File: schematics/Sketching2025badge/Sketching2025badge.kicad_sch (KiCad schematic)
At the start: 47 parts, among them J1 Conn_02x03, J2 Conn_01x04_Pin, SW1 Capacitive_Button, SW10 SSSS811101, SW2 Capacitive_Button, SW3 Capacitive_Button, U1 ATtiny816-M

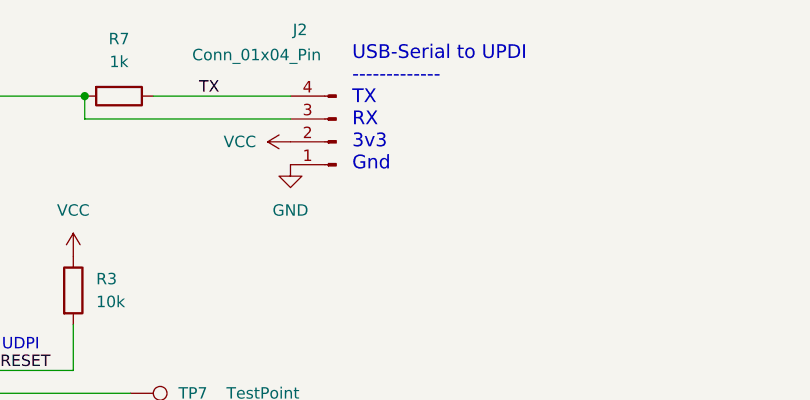
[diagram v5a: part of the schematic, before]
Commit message: moved to female prog header, widened mask polygons for more light
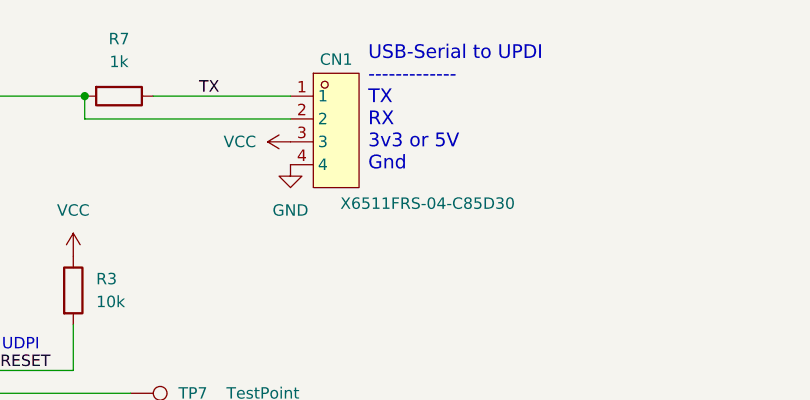
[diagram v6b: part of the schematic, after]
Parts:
- removed J2: Conn_01x04_Pin, Connector_Harwin:Harwin_M20-89004xx_1x04_P2.54mm_Horizontal, symbol Connector:Conn_01x04_Pin
- added CN1: X6511FRS-04-C85D30, easyeda2kicad:HDR-SMD_4P-P2.54-H-F, symbol easyeda2kicad:X6511FRS-04-C85D30
- J1: LCSC Part (none) -> C541853
- SW1, SW2, SW3, TP1, TP2, TP3, TP4: now left out of the parts list
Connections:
- net GND: now also CN1.4
- net RESET: now also CN1.2
- net TX: now also CN1.1
- net VCC: now also CN1.3
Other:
- note added: "USB-Serial to UPDI ------------- TX RX 3v3 or 5V Gnd"
- note removed: "USB-Serial to UPDI ------------- TX RX 3v3 Gnd"
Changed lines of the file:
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@@
 		)
 	)
-	(text "USB-Serial to UPDI\n-------------\nTX\nRX\n3v3\nGnd\n"
+	(text "USB-Serial to UPDI\n-------------\nTX\nRX\n3v3 or 5V\nGnd\n"
 		(exclude_from_sim no)
-		(at 221.488 24.892 0)
+		(at 223.266 24.892 0)
 		(effects
 			(font
@@
 	)
 	(symbol
-		(lib_id "Connector:Conn_01x04_Pin")
-		(at 219.71 35.56 180)
-		(unit 1)
-		(exclude_from_sim no)
-		(in_bom no)
-		(on_board yes)
-		(dnp no)
-		(property "Reference" "J2"
-			(at 214.884 23.114 0)
-			(effects
-				(font
-					(size 1.27 1.27)
-				)
-				(justify right)
-			)
-		)
-		(property "Value" "Conn_01x04_Pin"
-			(at 203.708 25.908 0)
-			(effects
-				(font
-					(size 1.27 1.27)
-				)
-				(justify right)
-			)
-		)
-		(property "Footprint" "Connector_Harwin:Harwin_M20-89004xx_1x04_P2.54mm_Horizontal"
-			(at 219.71 35.56 0)
-			(effects
-				(font
-					(size 1.27 1.27)
-				)
-				(hide yes)
-			)
-		)
-		(property "Datasheet" "~"
-			(at 219.71 35.56 0)
-			(effects
-				(font
-					(size 1.27 1.27)
-				)
-				(hide yes)
-			)
-		)
-		(property "Description" "Generic connector, single row, 01x04, script generated"
-			(at 219.71 35.56 0)
-			(effects
-				(font
-					(size 1.27 1.27)
-				)
-				(hide yes)
-			)
-		)
-		(pin "2"
-		)
-		(pin "3"
-		)
-		(pin "4"
-		)
-		(pin "1"
-		)
-		(instances
-			(project ""
-				(path "/598c645d-45d3-4f84-85f8-bbbc5b47d1f0"
-					(reference "J2")
-					(unit 1)
-				)
-			)
-		)
-	)
-	(symbol
 		(lib_id "power:VCC")
 		(at 223.52 154.94 0)
@@
 		(unit 1)
 		(exclude_from_sim no)
-		(in_bom yes)
+		(in_bom no)
 		(on_board yes)
 		(dnp no)
@@
 	)
 	(symbol
+		(lib_id "easyeda2kicad:X6511FRS-04-C85D30")
+		(at 219.71 34.29 0)
+		(unit 1)
+		(exclude_from_sim no)
+		(in_bom yes)
+		(on_board yes)
+		(dnp no)
+		(property "Reference" "CN1"
+			(at 219.71 26.416 0)
+			(effects
+				(font
+					(size 1.27 1.27)
+				)
+			)
+		)
+		(property "Value" "X6511FRS-04-C85D30"
+			(at 229.87 42.418 0)
+			(effects
+				(font
+					(size 1.27 1.27)
+				)
+			)
+		)
+		(property "Footprint" "easyeda2kicad:HDR-SMD_4P-P2.54-H-F"
+			(at 219.71 45.72 0)
+			(effects
+				(font
+					(size 1.27 1.27)
+				)
+				(hide yes)
+			)
+		)
+		(property "Datasheet" ""
+			(at 219.71 34.29 0)
+			(effects
+				(font
+					(size 1.27 1.27)
+				)
+				(hide yes)
+			)
+		)
+		(property "Description" ""
+			(at 219.71 34.29 0)
+			(effects
+				(font
+					(size 1.27 1.27)
+				)
+				(hide yes)
+			)
+		)
+		(property "LCSC Part" "C5142237"
+			(at 219.71 48.26 0)
+			(effects
+				(font
+					(size 1.27 1.27)
+				)
+				(hide yes)
+			)
+		)
+		(pin "1"
+		)
+		(pin "3"
+		)
+		(pin "4"
+		)
+		(pin "2"
+		)
+		(instances
+			(project ""
+				(path "/598c645d-45d3-4f84-85f8-bbbc5b47d1f0"
+					(reference "CN1")
+					(unit 1)
+				)
+			)
+		)
+	)
+	(symbol
 		(lib_id "easyeda2kicad:BH-AAA-A1AJ001")
 		(at 36.195 39.37 0)
@@
 		(unit 1)
 		(exclude_from_sim no)
-		(in_bom yes)
+		(in_bom no)
 		(on_board yes)
 		(dnp no)
@@
 		(unit 1)
 		(exclude_from_sim no)
-		(in_bom yes)
+		(in_bom no)
 		(on_board yes)
 		(dnp no)
@@
 		(unit 1)
 		(exclude_from_sim no)
-		(in_bom yes)
+		(in_bom no)
 		(on_board yes)
 		(dnp no)
@@
 		(unit 1)
 		(exclude_from_sim no)
-		(in_bom yes)
+		(in_bom no)
 		(on_board yes)
 		(dnp no)
@@
 			)
 		)
+		(property "LCSC Part" "C541853"
+			(at 93.98 72.39 90)
+			(effects
+				(font
+					(size 1.27 1.27)
+				)
+				(hide yes)
+			)
+		)
 		(pin "1"
 		)
@@
 		(unit 1)
 		(exclude_from_sim no)
-		(in_bom yes)
+		(in_bom no)
 		(on_board yes)
 		(dnp no)
@@
 		(unit 1)
 		(exclude_from_sim no)
-		(in_bom yes)
+		(in_bom no)
 		(on_board yes)
 		(dnp no)
